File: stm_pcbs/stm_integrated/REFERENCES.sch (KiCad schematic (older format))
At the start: 20 parts, among them U13 AD8676, U14 AD8675, U15 ADR445

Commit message: working on Kicad of 3rd Dec
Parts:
- C65, C66, C69, C70, C71, C74: symbol CP2 -> device:CP1
- C67, C68, C72, C73, C75, C76: symbol C -> device:C
- R5, R6, R7, R8, R9: symbol R -> device:R
- U13: symbol AD8676 -> ad5791:AD8676
- U14: symbol AD8675 -> ad5791:AD8675
- U15: symbol adr445 -> adr445:adr445
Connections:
- wire segments 65 -> 81

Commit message: fixing more borkage
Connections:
- wire segments 81 -> 77
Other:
- moved on the sheet: C70, C71, C72, C73, C74

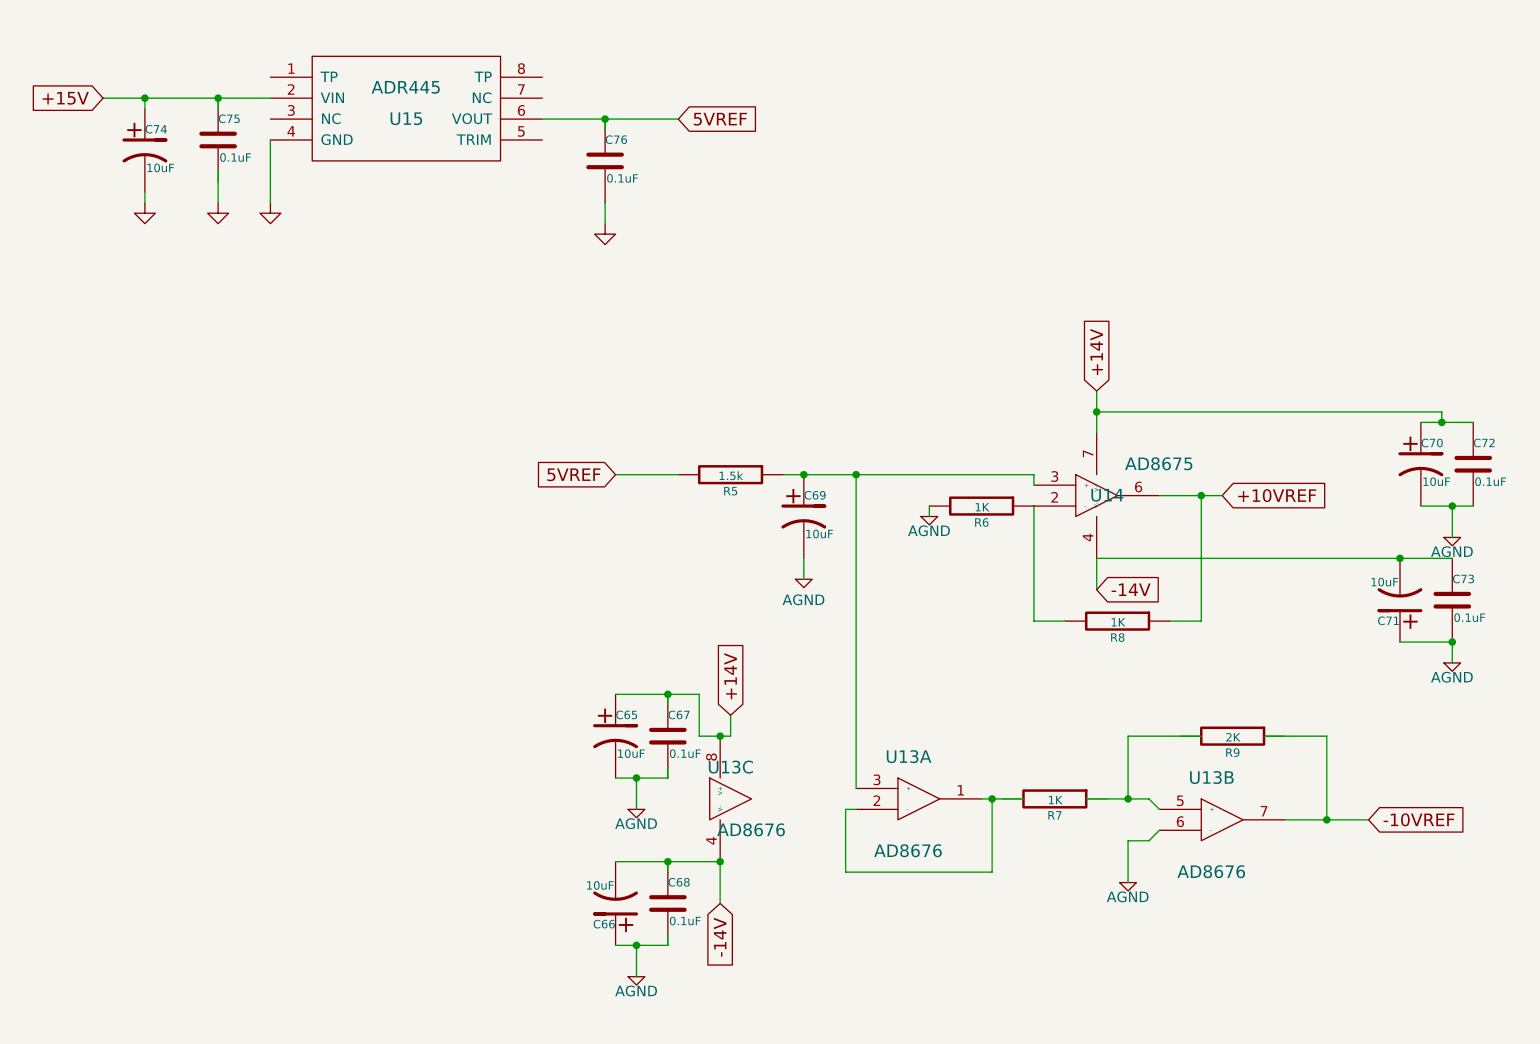
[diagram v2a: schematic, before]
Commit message: tidying up boards, adding all DAC signals.
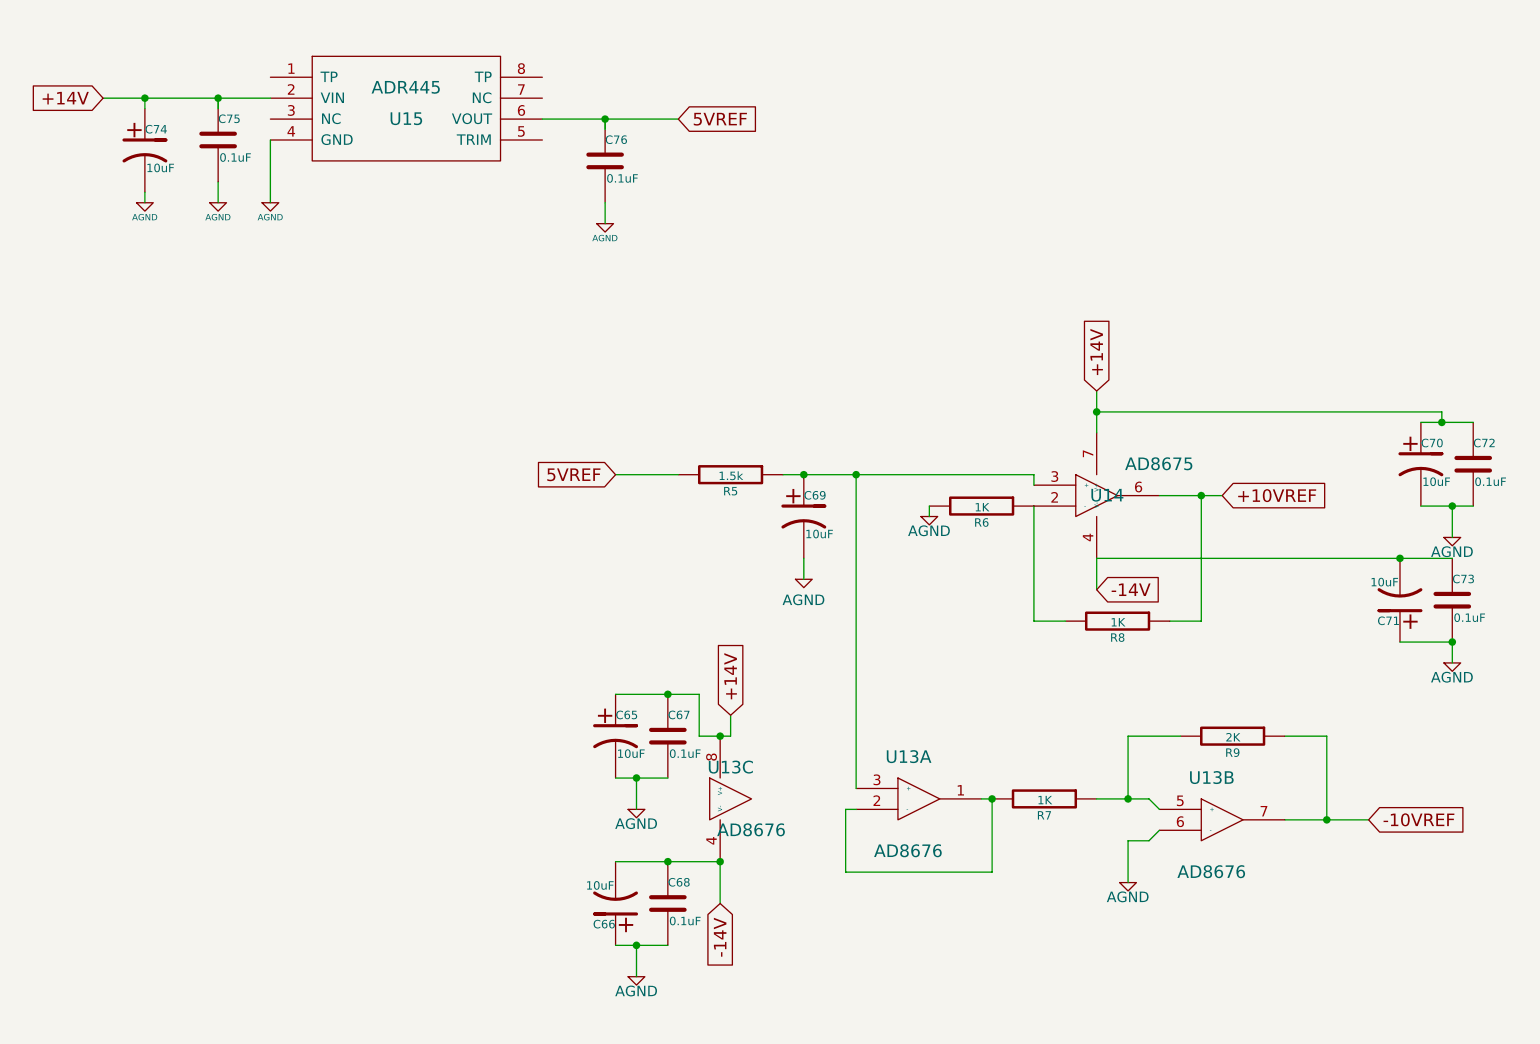
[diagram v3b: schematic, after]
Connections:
- net labels removed: +15V, GND
- wire segments 77 -> 72
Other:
- moved on the sheet: R7
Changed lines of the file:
@@
 L device:R R7
 U 1 1 5A25B573
-P 5800 4500
+P 5750 4500
 AR Path="/5A25B573" Ref="R7"  Part="1"
 AR Path="/5A25A477/5A25B573" Ref="R7"  Part="1"
-F 0 "R7" V 5880 4500 40  0000 C CNN
-F 1 "1K" V 5807 4501 40  0000 C CNN
-F 2 "Resistors_SMD:R_0805_HandSoldering" V 5730 4500 30  0001 C CNN
-F 3 "" H 5800 4500 30  0000 C CNN
-	1    5800 4500
+F 0 "R7" V 5830 4500 40  0000 C CNN
+F 1 "1K" V 5757 4501 40  0000 C CNN
+F 2 "Resistors_SMD:R_0805_HandSoldering" V 5680 4500 30  0001 C CNN
+F 3 "" H 5750 4500 30  0000 C CNN
+	1    5750 4500
 	0    1    1    0
 $EndComp
@@
 	5450 4500 5500 4500
 Wire Wire Line
-	5950 4500 6150 4500
-Wire Wire Line
 	6150 4700 6150 4900
 Wire Wire Line
 	6150 4200 6150 4500
 Wire Wire Line
-	6150 4200 6500 4200
+	6150 4200 6400 4200
 Connection ~ 6500 3050
 Wire Wire Line
@@
 	7100 4200 7100 4600
 Connection ~ 7100 4600
-Wire Wire Line
-	6800 4200 7100 4200
-Wire Wire Line
-	3950 4400 3950 4350
-Wire Wire Line
-	3950 4050 3950 4000
-Wire Wire Line
-	3950 4800 3950 4850
-Wire Wire Line
-	3950 5200 3950 5150
 Connection ~ 6000 2650
 Wire Wire Line
@@
 $EndComp
 Text GLabel 1250 1150 0    60   Input ~ 0
-+15V
++14V
 Text GLabel 4000 1250 2    60   Input ~ 0
 5VREF
@@
 $EndComp
 $Comp
-L power:GND #PWR056
+L power:AGND #PWR056
 U 1 1 5A22E9A1
 P 1800 1650
@@
 AR Path="/5A25A477/5A22E9A1" Ref="#PWR056"  Part="1"
 F 0 "#PWR056" H 1800 1650 30  0001 C CNN
-F 1 "GND" H 1800 1580 30  0001 C CNN
+F 1 "AGND" H 1800 1580 30  0000 C CNN
 F 2 "" H 1800 1650 60  0000 C CNN
 F 3 "" H 1800 1650 60  0000 C CNN
@@
 $EndComp
 $Comp
-L power:GND #PWR057
+L power:AGND #PWR057
 U 1 1 5A22E9A7
 P 1450 1650
@@
 AR Path="/5A25A477/5A22E9A7" Ref="#PWR057"  Part="1"
 F 0 "#PWR057" H 1450 1650 30  0001 C CNN
-F 1 "GND" H 1450 1580 30  0001 C CNN
+F 1 "AGND" H 1450 1580 30  0000 C CNN
 F 2 "" H 1450 1650 60  0000 C CNN
 F 3 "" H 1450 1650 60  0000 C CNN
@@
 $EndComp
 $Comp
-L power:GND #PWR058
+L power:AGND #PWR058
 U 1 1 5A22E9AD
 P 2050 1650
@@
 AR Path="/5A25A477/5A22E9AD" Ref="#PWR058"  Part="1"
 F 0 "#PWR058" H 2050 1650 30  0001 C CNN
-F 1 "GND" H 2050 1580 30  0001 C CNN
+F 1 "AGND" H 2050 1580 30  0000 C CNN
 F 2 "" H 2050 1650 60  0000 C CNN
 F 3 "" H 2050 1650 60  0000 C CNN
@@
 $EndComp
 $Comp
-L power:GND #PWR059
+L power:AGND #PWR059
 U 1 1 5A22E9BA
 P 3650 1750
@@
 AR Path="/5A25A477/5A22E9BA" Ref="#PWR059"  Part="1"
 F 0 "#PWR059" H 3650 1750 30  0001 C CNN
-F 1 "GND" H 3650 1680 30  0001 C CNN
+F 1 "AGND" H 3650 1680 30  0000 C CNN
 F 2 "" H 3650 1750 60  0000 C CNN
 F 3 "" H 3650 1750 60  0000 C CNN
@@
 	1450 1650 1450 1600
 Wire Wire Line
-	1800 1500 1800 1650
-Wire Wire Line
 	3350 1250 3650 1250
 Wire Wire Line
@@
 Wire Wire Line
 	3950 4000 4100 4000
-Wire Wire Line
-	5500 4500 5650 4500
 Wire Wire Line
 	6150 4500 6250 4500
@@
 Wire Wire Line
 	7650 2700 7800 2700
+Wire Wire Line
+	6900 4200 7100 4200
+Wire Wire Line
+	6000 4500 6150 4500
+Wire Wire Line
+	1800 1550 1800 1650
 $EndSCHEMATC

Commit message: Using LTZ1000 (A9 board)
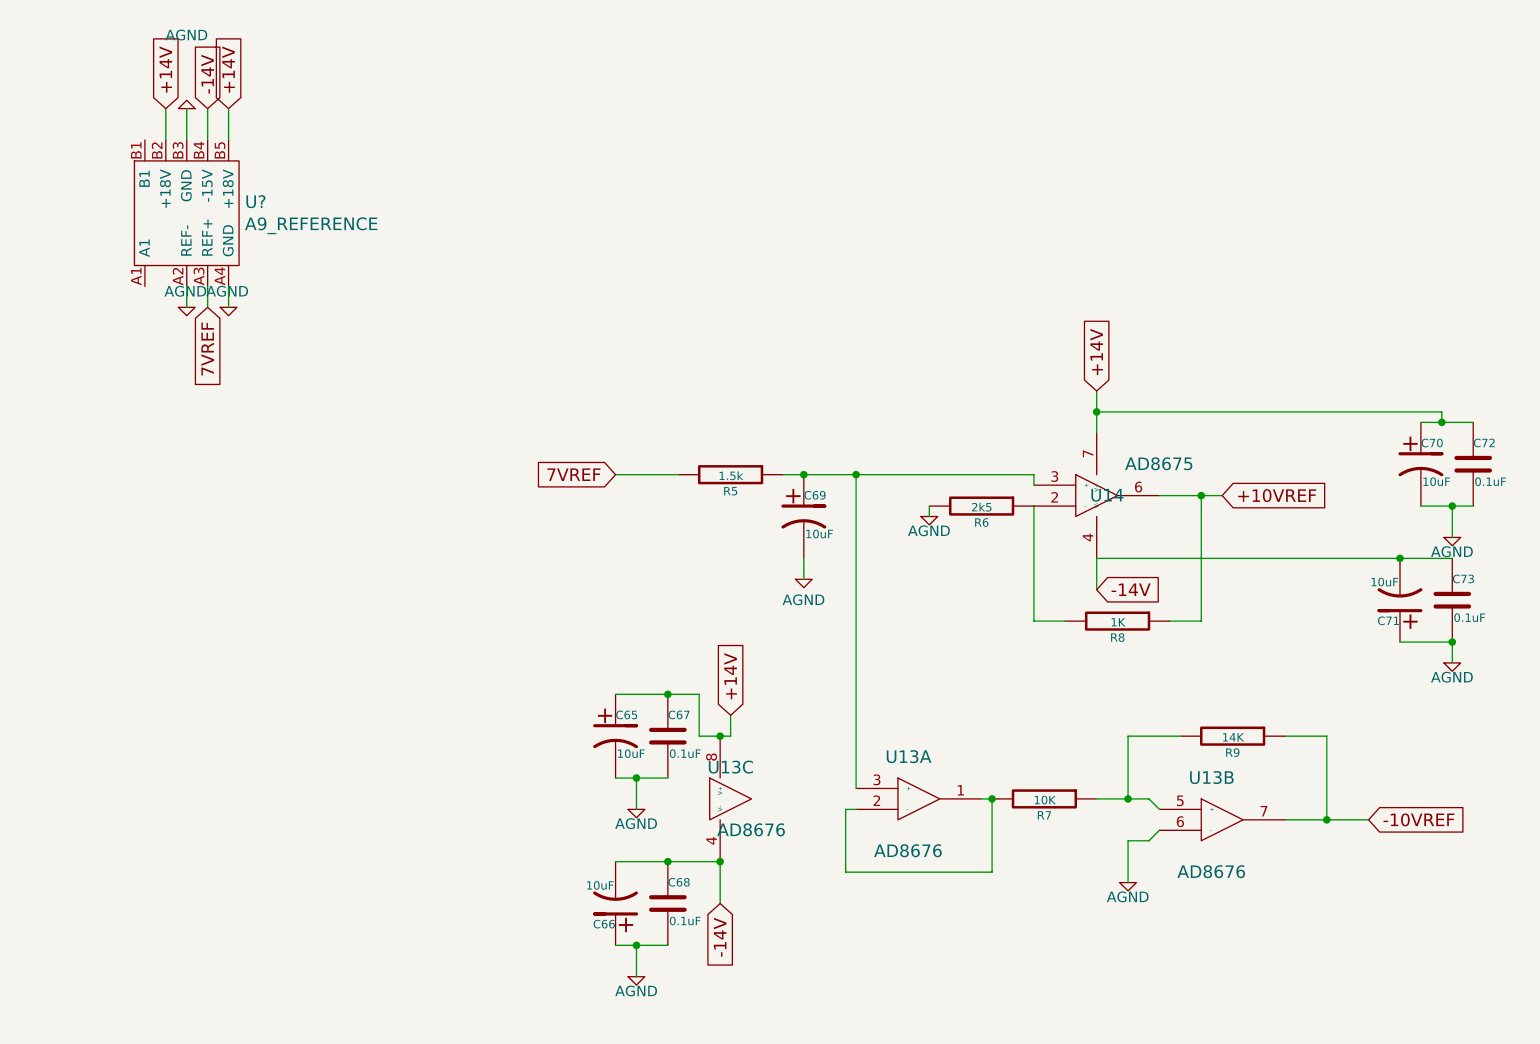
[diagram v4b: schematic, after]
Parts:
- removed C74: 10uF, stm:SMD-1210_Pol, symbol device:CP1
- removed C75: 0.1uF, Capacitors_SMD:C_0805, symbol device:C
- removed C76: 0.1uF, stm:SMD-1210_Pol, symbol device:C
- removed U15: ADR445, SMD_Packages:SOIC-8-N, symbol adr445:adr445
- added U?: A9_REFERENCE, symbol A9_REFERENCE:A9_REFERENCE
- R6: value 1K -> 2k5
- R7: value 1K -> 10K
- R9: value 2K -> 14K
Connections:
- net labels added: 7VREF
- net labels removed: 5VREF
- wire segments 72 -> 67
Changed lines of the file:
@@
 AR Path="/5A25A477/5A25B565" Ref="R6"  Part="1"
 F 0 "R6" V 5530 3100 40  0000 C CNN
-F 1 "1K" V 5457 3101 40  0000 C CNN
+F 1 "2k5" V 5457 3101 40  0000 C CNN
 F 2 "Resistors_SMD:R_0805_HandSoldering" V 5380 3100 30  0001 C CNN
 F 3 "" H 5450 3100 30  0000 C CNN
@@
 AR Path="/5A25A477/5A25B573" Ref="R7"  Part="1"
 F 0 "R7" V 5830 4500 40  0000 C CNN
-F 1 "1K" V 5757 4501 40  0000 C CNN
+F 1 "10K" V 5757 4501 40  0000 C CNN
 F 2 "Resistors_SMD:R_0805_HandSoldering" V 5680 4500 30  0001 C CNN
 F 3 "" H 5750 4500 30  0000 C CNN
@@
 AR Path="/5A25A477/5A25B586" Ref="R9"  Part="1"
 F 0 "R9" V 6730 4200 40  0000 C CNN
-F 1 "2K" V 6657 4201 40  0000 C CNN
+F 1 "14K" V 6657 4201 40  0000 C CNN
 F 2 "Resistors_SMD:R_0805_HandSoldering" V 6580 4200 30  0001 C CNN
 F 3 "" H 6650 4200 30  0000 C CNN
@@
 +10VREF
 Text GLabel 3700 2950 0    60   Input ~ 0
-5VREF
+7VREF
 Text GLabel 6000 2550 1    60   Input ~ 0
 +14V
@@
 Wire Wire Line
 	4600 3450 4600 3350
-$Comp
-L adr445:adr445 U15
-U 1 1 5A22E991
-P 2700 1200
-AR Path="/5A22E991" Ref="U15"  Part="1"
-AR Path="/5A25A477/5A22E991" Ref="U15"  Part="1"
-F 0 "U15" H 2700 1150 60  0000 C CNN
-F 1 "ADR445" H 2700 1300 60  0000 C CNN
-F 2 "SMD_Packages:SOIC-8-N" H 2700 1200 60  0001 C CNN
-F 3 "" H 2700 1200 60  0000 C CNN
-	1    2700 1200
-	1    0    0    -1
-$EndComp
-Text GLabel 1250 1150 0    60   Input ~ 0
-+14V
-Text GLabel 4000 1250 2    60   Input ~ 0
-5VREF
-$Comp
-L device:C C75
-U 1 1 5A22E99A
-P 1800 1350
-AR Path="/5A22E99A" Ref="C75"  Part="1"
-AR Path="/5A25A477/5A22E99A" Ref="C75"  Part="1"
-F 0 "C75" H 1800 1450 40  0000 L CNN
-F 1 "0.1uF" H 1806 1265 40  0000 L CNN
-F 2 "Capacitors_SMD:C_0805" H 1838 1200 30  0001 C CNN
-F 3 "" H 1800 1350 60  0000 C CNN
-	1    1800 1350
-	1    0    0    -1
-$EndComp
-$Comp
-L power:AGND #PWR056
-U 1 1 5A22E9A1
-P 1800 1650
-AR Path="/5A22E9A1" Ref="#PWR056"  Part="1"
-AR Path="/5A25A477/5A22E9A1" Ref="#PWR056"  Part="1"
-F 0 "#PWR056" H 1800 1650 30  0001 C CNN
-F 1 "AGND" H 1800 1580 30  0000 C CNN
-F 2 "" H 1800 1650 60  0000 C CNN
-F 3 "" H 1800 1650 60  0000 C CNN
-	1    1800 1650
-	1    0    0    -1
-$EndComp
-$Comp
-L power:AGND #PWR057
-U 1 1 5A22E9A7
-P 1450 1650
-AR Path="/5A22E9A7" Ref="#PWR057"  Part="1"
-AR Path="/5A25A477/5A22E9A7" Ref="#PWR057"  Part="1"
-F 0 "#PWR057" H 1450 1650 30  0001 C CNN
-F 1 "AGND" H 1450 1580 30  0000 C CNN
-F 2 "" H 1450 1650 60  0000 C CNN
-F 3 "" H 1450 1650 60  0000 C CNN
-	1    1450 1650
-	1    0    0    -1
-$EndComp
-$Comp
-L power:AGND #PWR058
-U 1 1 5A22E9AD
-P 2050 1650
-AR Path="/5A22E9AD" Ref="#PWR058"  Part="1"
-AR Path="/5A25A477/5A22E9AD" Ref="#PWR058"  Part="1"
-F 0 "#PWR058" H 2050 1650 30  0001 C CNN
-F 1 "AGND" H 2050 1580 30  0000 C CNN
-F 2 "" H 2050 1650 60  0000 C CNN
-F 3 "" H 2050 1650 60  0000 C CNN
-	1    2050 1650
-	1    0    0    -1
-$EndComp
-$Comp
-L device:C C76
-U 1 1 5A22E9B3
-P 3650 1450
-AR Path="/5A22E9B3" Ref="C76"  Part="1"
-AR Path="/5A25A477/5A22E9B3" Ref="C76"  Part="1"
-F 0 "C76" H 3650 1550 40  0000 L CNN
-F 1 "0.1uF" H 3656 1365 40  0000 L CNN
-F 2 "stm:SMD-1210_Pol" H 3688 1300 30  0001 C CNN
-F 3 "" H 3650 1450 60  0000 C CNN
-	1    3650 1450
-	1    0    0    -1
-$EndComp
-$Comp
-L power:AGND #PWR059
-U 1 1 5A22E9BA
-P 3650 1750
-AR Path="/5A22E9BA" Ref="#PWR059"  Part="1"
-AR Path="/5A25A477/5A22E9BA" Ref="#PWR059"  Part="1"
-F 0 "#PWR059" H 3650 1750 30  0001 C CNN
-F 1 "AGND" H 3650 1680 30  0000 C CNN
-F 2 "" H 3650 1750 60  0000 C CNN
-F 3 "" H 3650 1750 60  0000 C CNN
-	1    3650 1750
-	1    0    0    -1
-$EndComp
-$Comp
-L device:CP1 C74
-U 1 1 5A22E9C0
-P 1450 1400
-AR Path="/5A22E9C0" Ref="C74"  Part="1"
-AR Path="/5A25A477/5A22E9C0" Ref="C74"  Part="1"
-F 0 "C74" H 1450 1500 40  0000 L CNN
-F 1 "10uF" H 1456 1315 40  0000 L CNN
-F 2 "stm:SMD-1210_Pol" H 1488 1250 30  0001 C CNN
-F 3 "" H 1450 1400 60  0000 C CNN
-	1    1450 1400
-	1    0    0    -1
-$EndComp
-Connection ~ 3650 1250
-Connection ~ 1800 1150
-Wire Wire Line
-	2050 1350 2050 1650
-Wire Wire Line
-	1450 1650 1450 1600
-Wire Wire Line
-	3350 1250 3650 1250
-Wire Wire Line
-	3650 1300 3650 1250
-Wire Wire Line
-	1800 1200 1800 1150
 Wire Wire Line
 	4850 2950 5700 2950
@@
 Wire Wire Line
 	7700 3100 7700 3250
-Wire Wire Line
-	3650 1250 4000 1250
-Wire Wire Line
-	1800 1150 2050 1150
-Wire Wire Line
-	1250 1150 1450 1150
-Wire Wire Line
-	1450 1200 1450 1150
-Connection ~ 1450 1150
-Wire Wire Line
-	1450 1150 1800 1150
-Wire Wire Line
-	3650 1750 3650 1650
 $Comp
 L device:CP1 C69
@@
 Wire Wire Line
 	6000 4500 6150 4500
-Wire Wire Line
-	1800 1550 1800 1650
+Text GLabel 1850 1200 1    60   Input ~ 0
++14V
+$Comp
+L LTC1859:AGND #PWR?
+U 1 1 5A2C3626
+P 1650 1200
+F 0 "#PWR?" H 1650 1200 40  0001 C CNN
+F 1 "AGND" H 1650 850 50  0000 C CNN
+F 2 "" H 1650 1200 60  0000 C CNN
+F 3 "" H 1650 1200 60  0000 C CNN
+	1    1650 1200
+	-1   0    0    1
+$EndComp
+Text GLabel 1750 1200 1    60   Input ~ 0
+-14V
+Text GLabel 1550 1200 1    60   Input ~ 0
++14V
+$Comp
+L LTC1859:AGND #PWR?
+U 1 1 5A2CA845
+P 1850 2150
+F 0 "#PWR?" H 1850 2150 40  0001 C CNN
+F 1 "AGND" H 1845 2225 50  0000 C CNN
+F 2 "" H 1850 2150 60  0000 C CNN
+F 3 "" H 1850 2150 60  0000 C CNN
+	1    1850 2150
+	1    0    0    -1
+$EndComp
+Text GLabel 1750 2150 3    60   Input ~ 0
+7VREF
+$Comp
+L LTC1859:AGND #PWR?
+U 1 1 5A2CCBC6
+P 1650 2150
+F 0 "#PWR?" H 1650 2150 40  0001 C CNN
+F 1 "AGND" H 1645 2225 50  0000 C CNN
+F 2 "" H 1650 2150 60  0000 C CNN
+F 3 "" H 1650 2150 60  0000 C CNN
+	1    1650 2150
+	1    0    0    -1
+$EndComp
+$Comp
+L A9_REFERENCE:A9_REFERENCE U?
+U 1 1 5A2A6FA3
+P 1650 1700
+F 0 "U?" H 1928 1753 60  0000 L CNN
+F 1 "A9_REFERENCE" H 1928 1647 60  0000 L CNN
+F 2 "" H 1650 1700 60  0001 C CNN
+F 3 "" H 1650 1700 60  0001 C CNN
+	1    1650 1700
+	1    0    0    -1
+$EndComp
+Wire Wire Line
+	1850 1200 1850 1350
+Wire Wire Line
+	1750 1350 1750 1200
+Wire Wire Line
+	1650 1200 1650 1350
+Wire Wire Line
+	1550 1350 1550 1200
+Wire Wire Line
+	1650 2150 1650 2050
+Wire Wire Line
+	1850 2150 1850 2050
+Wire Wire Line
+	1750 2150 1750 2050
 $EndSCHEMATC
